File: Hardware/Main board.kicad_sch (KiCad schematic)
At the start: 38 parts, among them U1 ESP32-S3, Y1 R940000171

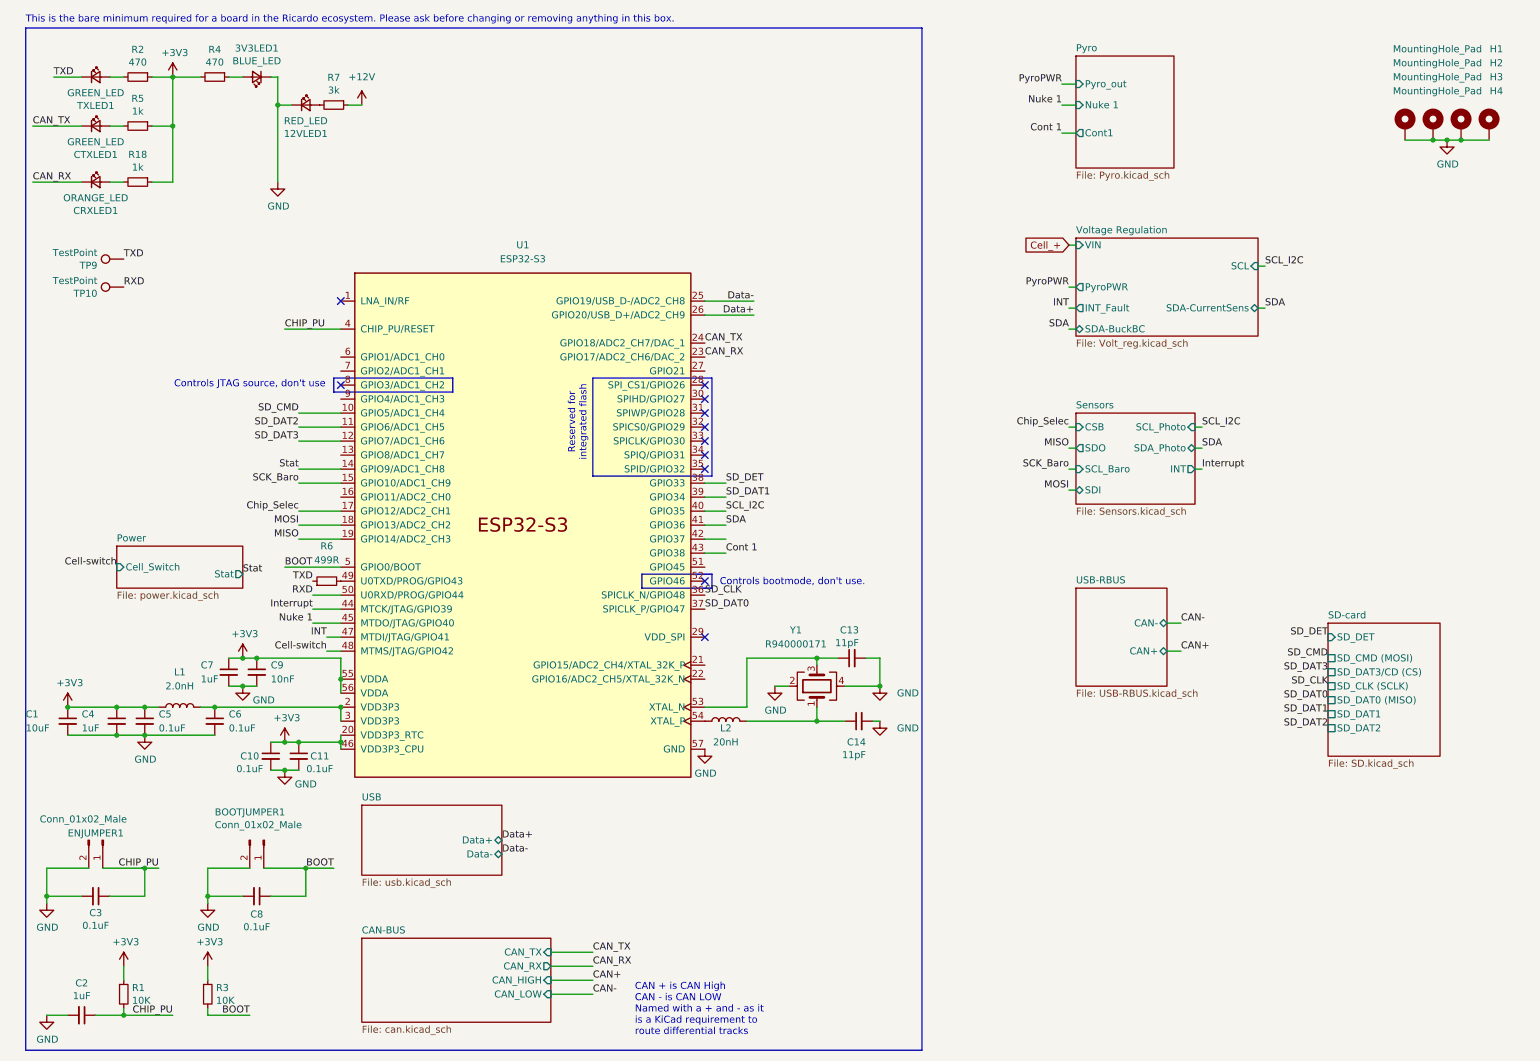
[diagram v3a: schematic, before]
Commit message: GPIO broken out + post review 4
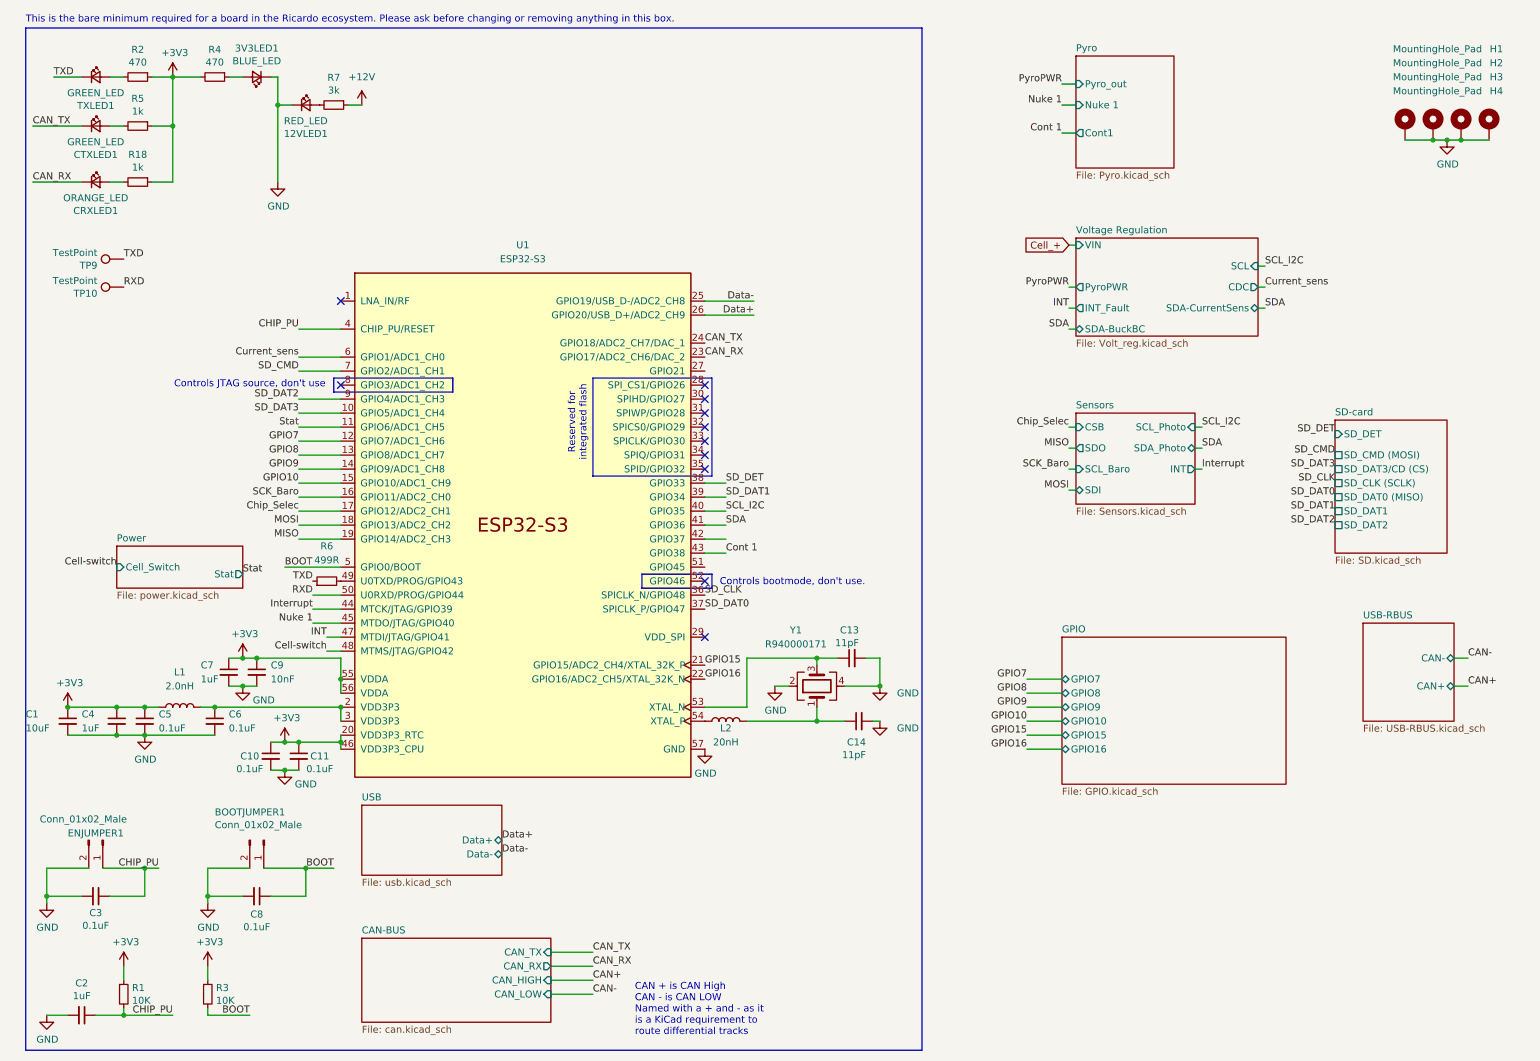
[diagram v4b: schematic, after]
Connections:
- net SCK_Baro: now also U1.16 (GPIO11/ADC2_CH0); no longer U1.15 (GPIO10/ADC1_CH9)
- net SD_CMD: now also U1.7 (GPIO2/ADC1_CH1); no longer U1.10 (GPIO5/ADC1_CH4)
- net SD_DAT2: now also U1.9 (GPIO4/ADC1_CH3); no longer U1.11 (GPIO6/ADC1_CH5)
- net SD_DAT3: now also U1.10 (GPIO5/ADC1_CH4); no longer U1.12 (GPIO7/ADC1_CH6)
- net Stat: now also U1.11 (GPIO6/ADC1_CH5); no longer U1.14 (GPIO9/ADC1_CH8)
- net GPIO8: now reaches U1.13 (GPIO8/ADC1_CH7)
- net GPIO15: now reaches U1.21 (GPIO15/ADC2_CH4/XTAL_32K_P)
- net GPIO16: now reaches U1.22 (GPIO16/ADC2_CH5/XTAL_32K_N)
- net Current_sens: now reaches U1.6 (GPIO1/ADC1_CH0)
- new net GPIO10: U1.15 (GPIO10/ADC1_CH9)
- new net GPIO7: U1.12 (GPIO7/ADC1_CH6)
- new net GPIO9: U1.14 (GPIO9/ADC1_CH8)
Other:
- added sheet GPIO (GPIO.kicad_sch)
- sheet Voltage Regulation ports: added CDC; removed none

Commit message: Extra tweaks - current sense etc
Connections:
- net GPIO15: no longer names the net of U1.21 (GPIO15/ADC2_CH4/XTAL_32K_P)
- net GPIO16: no longer names the net of U1.22 (GPIO16/ADC2_CH5/XTAL_32K_N)
- no-connect marks 11 -> 15
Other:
- sheet GPIO ports: added none; removed GPIO15, GPIO16
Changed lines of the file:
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@@
 	)
 	(no_connect
+		(at 135.89 74.93)
+	)
+	(no_connect
 		(at 135.89 85.09)
 	)
@@
 	)
 	(no_connect
+		(at 135.89 130.81)
+	)
+	(no_connect
 		(at 135.89 92.71)
 	)
@@
 		(at 135.89 123.19)
 	)
+	(no_connect
+		(at 135.89 110.49)
+	)
+	(no_connect
+		(at 135.89 128.27)
+	)
 	(wire
 		(pts
@@
 	(wire
 		(pts
-			(xy 194.31 143.51) (xy 200.66 143.51)
-		)
-		(stroke
-			(width 0)
-			(type default)
-		)
-	)
-	(wire
-		(pts
 			(xy 224.79 92.71) (xy 226.06 92.71)
 		)
@@
 	(wire
 		(pts
-			(xy 194.31 140.97) (xy 200.66 140.97)
-		)
-		(stroke
-			(width 0)
-			(type default)
-		)
-	)
-	(wire
-		(pts
 			(xy 49.53 132.08) (xy 52.07 132.08)
 		)
@@
 		)
 	)
-	(label "GPIO15"
-		(at 194.31 140.97 180)
-		(effects
-			(font
-				(size 1.27 1.27)
-			)
-			(justify right bottom)
-		)
-	)
 	(label "SD_DET"
 		(at 139.7 95.25 0)
@@
 		)
 	)
-	(label "GPIO16"
-		(at 194.31 143.51 180)
-		(effects
-			(font
-				(size 1.27 1.27)
-			)
-			(justify right bottom)
-		)
-	)
 	(label "GPIO9"
 		(at 62.23 92.71 180)
@@
 		)
 	)
-	(label "GPIO15"
-		(at 135.89 128.27 0)
-		(effects
-			(font
-				(size 1.27 1.27)
-			)
-			(justify left bottom)
-		)
-	)
 	(label "CAN_RX"
 		(at 115.57 182.88 0)
@@
 		)
 	)
-	(label "GPIO16"
-		(at 135.89 130.81 0)
-		(effects
-			(font
-				(size 1.27 1.27)
-			)
-			(justify left bottom)
-		)
-	)
 	(label "TXD"
 		(at 17.78 21.59 0)
@@
 			(effects
 				(font
-					(size 1.27 1.27)
-				)
-				(justify left)
-			)
-		)
-		(pin "GPIO15" bidirectional
-			(at 200.66 140.97 180)
-			(effects
-				(font
-					(size 1.27 1.27)
-				)
-				(justify left)
-			)
-		)
-		(pin "GPIO16" bidirectional
-			(at 200.66 143.51 180)
-			(effects
-				(font

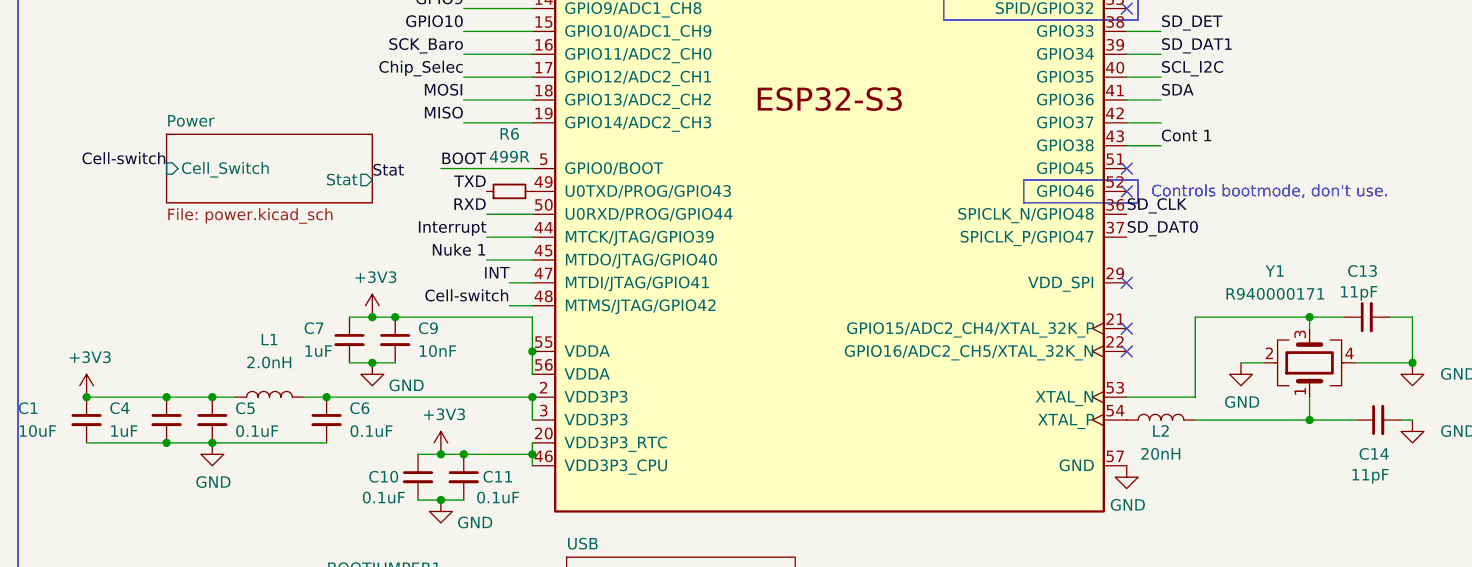
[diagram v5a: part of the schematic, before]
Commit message: Added voltage ref for post ideal diode
(more firmware too)
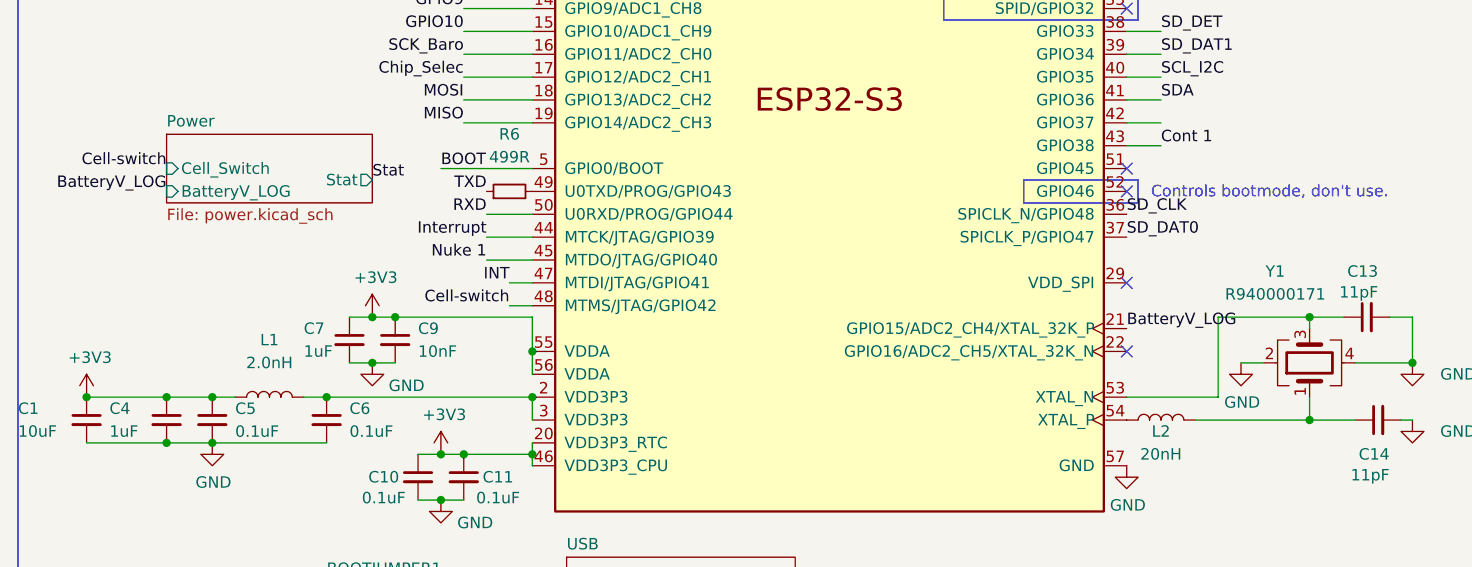
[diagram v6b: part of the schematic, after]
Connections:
- net BatteryV_LOG: now reaches U1.21 (GPIO15/ADC2_CH4/XTAL_32K_P)
- no-connect marks 15 -> 14
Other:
- sheet Power ports: added BatteryV_LOG; removed none
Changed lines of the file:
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@@
 		(at 135.89 110.49)
 	)
-	(no_connect
-		(at 135.89 128.27)
-	)
 	(wire
 		(pts
@@
 	(wire
 		(pts
-			(xy 143.51 135.89) (xy 143.51 127)
+			(xy 146.05 135.89) (xy 146.05 127)
 		)
 		(stroke
@@
 	(wire
 		(pts
-			(xy 135.89 135.89) (xy 143.51 135.89)
+			(xy 135.89 135.89) (xy 146.05 135.89)
 		)
 		(stroke
@@
 	(wire
 		(pts
-			(xy 143.51 127) (xy 156.21 127)
+			(xy 146.05 127) (xy 156.21 127)
 		)
 		(stroke
@@
 		)
 	)
+	(label "BatteryV_LOG"
+		(at 135.89 128.27 0)
+		(effects
+			(font
+				(size 1.27 1.27)
+			)
+			(justify left bottom)
+		)
+	)
 	(label "Interrupt "
 		(at 64.77 118.11 180)
@@
 		)
 	)
+	(label "BatteryV_LOG"
+		(at 29.21 113.03 180)
+		(effects
+			(font
+				(size 1.27 1.27)
+			)
+			(justify right bottom)
+		)
+	)
 	(global_label "Cell_+"
 		(shape input)
@@
 			(effects
 				(font
+					(size 1.27 1.27)
+				)
+				(justify left)
+			)
+		)
+		(pin "BatteryV_LOG" input
+			(at 29.21 113.03 180)
+			(effects
+				(font

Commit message: Mega commit
Post review changes
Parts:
- removed 12VLED1: RED_LED, Resistor_SMD:R_0402_1005Metric, symbol Device:LED_Small
- removed R7: 3k, Resistor_SMD:R_0402_1005Metric, symbol Device:R_Small
- 3V3LED1, CRXLED1, CTXLED1, TXLED1: footprint Resistor_SMD:R_0402_1005Metric -> LED_SMD:LED_0402_1005Metric
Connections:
- net Interrupt  is gone; now on net Cont 1: U1.44 (MTCK/JTAG/GPIO39)
- net Stat is gone; now on net GPIO7: U1.11 (GPIO6/ADC1_CH5)
- net Cont 1: no longer U1.43 (GPIO38)
- net Current_sens: now also U1.45 (MTDO/JTAG/GPIO40); no longer U1.6 (GPIO1/ADC1_CH0)
- net GPIO10: now also U1.14 (GPIO9/ADC1_CH8); no longer U1.15 (GPIO10/ADC1_CH9)
- net GPIO7: no longer U1.12 (GPIO7/ADC1_CH6)
- net GPIO8: now also U1.12 (GPIO7/ADC1_CH6); no longer U1.13 (GPIO8/ADC1_CH7)
- net GPIO9: now also U1.13 (GPIO8/ADC1_CH7); no longer U1.14 (GPIO9/ADC1_CH8)
- net Nuke 1: now also U1.43 (GPIO38); no longer U1.45 (MTDO/JTAG/GPIO40)
- net Interrupt_photo: now reaches U1.42 (GPIO37)
- net Chip_Selec renamed CS_Baro
- net INT renamed BuckBoost_INT
- net MISO renamed MISO_Baro
- net MOSI renamed MOSI_Baro
- new net DeployV_LOG: U1.15 (GPIO10/ADC1_CH9)
- new net ID_Stat: U1.6 (GPIO1/ADC1_CH0)
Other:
- sheet Power ports: added DeployV_LOG, ID_Stat; removed Stat
- sheet Sensors ports: added CS_Baro, SDI_Baro, SDO_Baro; removed CSB, SDI, SDO
- note added: "ADD TO ESP32S3 CONNECTOR"
